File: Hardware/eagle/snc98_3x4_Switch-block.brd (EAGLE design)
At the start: 56.4 x 83.2 mm, 67 parts

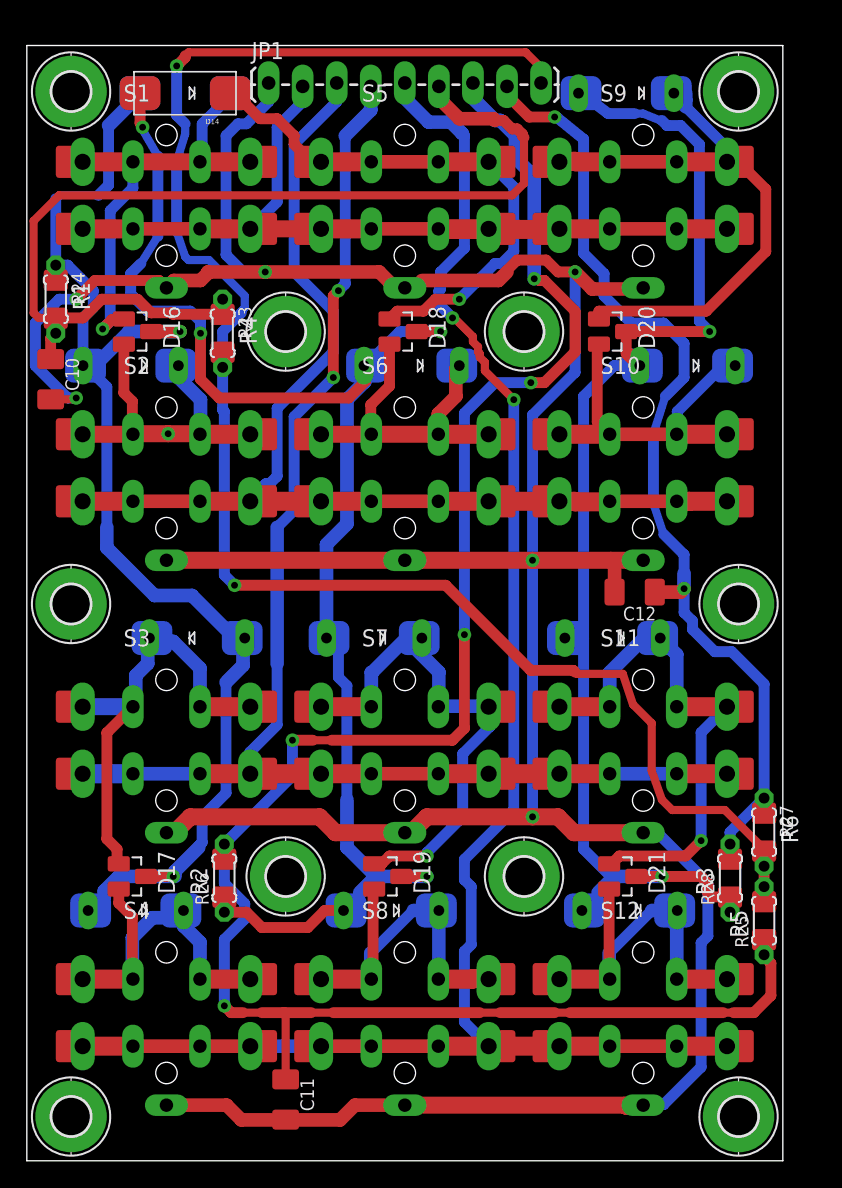
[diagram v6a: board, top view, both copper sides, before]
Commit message: new Switch Layout - with Kipptaster
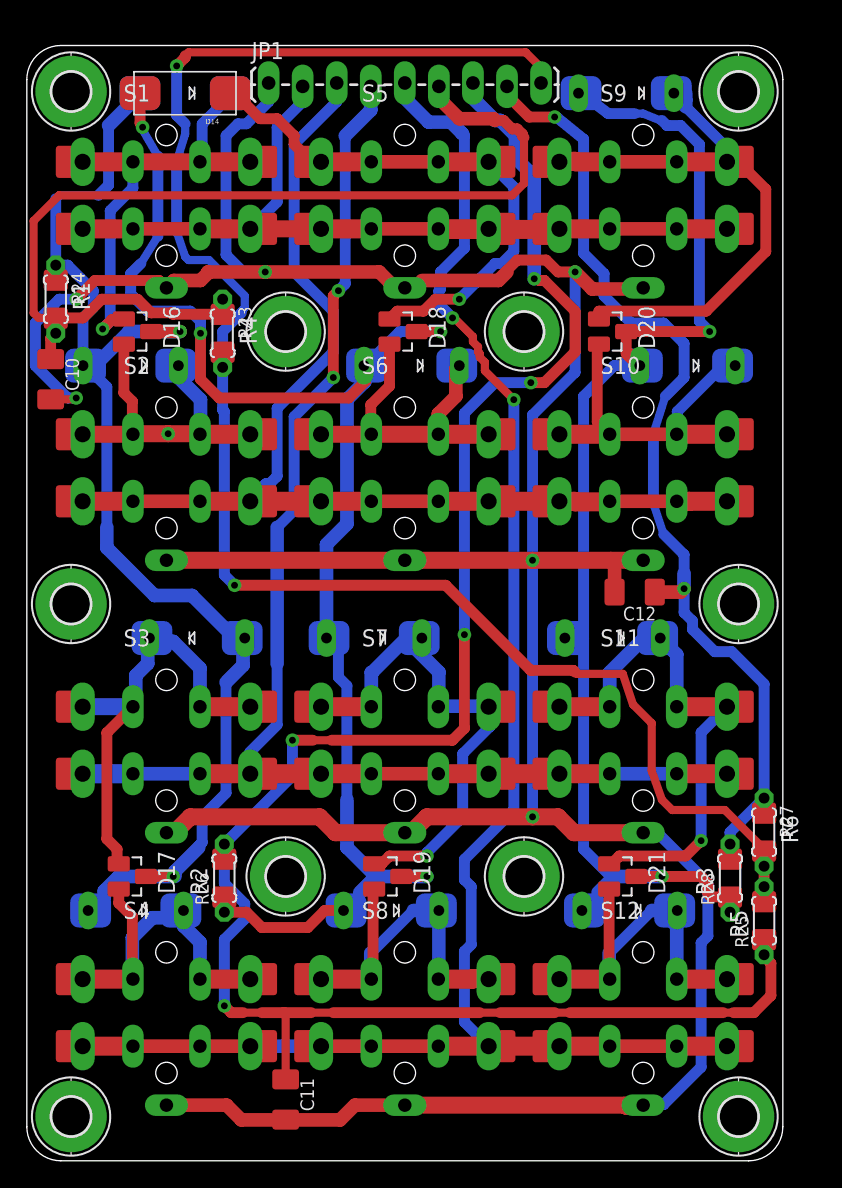
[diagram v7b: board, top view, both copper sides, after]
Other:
- outline, holes or cut-outs redrawn
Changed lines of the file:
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@@
 <setting verticaltext="up"/>
 </settings>
-<grid distance="5" unitdist="mil" unit="mil" style="dots" multiple="1" display="yes" altdistance="0.005" altunitdist="inch" altunit="inch"/>
+<grid distance="5" unitdist="mil" unit="mil" style="lines" multiple="1" display="yes" altdistance="0.01" altunitdist="inch" altunit="inch"/>
 <layers>
 <layer number="1" name="Top" color="4" fill="1" visible="yes" active="yes"/>
@@
 <board>
 <plain>
-<wire x1="0" y1="83.185" x2="0" y2="0" width="0" layer="20"/>
-<wire x1="0" y1="0" x2="56.388" y2="0" width="0" layer="20"/>
+<wire x1="0" y1="2.54" x2="0" y2="80.645" width="0" layer="20"/>
+<wire x1="2.54" y1="83.185" x2="53.848" y2="83.185" width="0" layer="20"/>
+<wire x1="56.388" y1="80.645" x2="56.388" y2="2.54" width="0" layer="20"/>
+<wire x1="2.54" y1="0" x2="53.848" y2="0" width="0" layer="20"/>
 <text x="7.874" y="42.164" size="1.27" layer="22" ratio="16" rot="MR180">snc98 3x4 Switch-block Rev. 0.3</text>
 <text x="37.846" y="42.545" size="1.27" layer="22" ratio="16" rot="MR0">CERN OHL    v.1.2 or later</text>
@@
 <text x="2.159" y="23.114" size="1.27" layer="22" ratio="16" rot="MR270" align="center">source</text>
 <text x="27.94" y="1.397" size="1.27" layer="22" ratio="16" rot="MR0" align="center">https://oshpark.com/profiles/Jens_G</text>
-<wire x1="0" y1="83.185" x2="56.388" y2="83.185" width="0" layer="20"/>
-<wire x1="56.388" y1="83.185" x2="56.388" y2="0" width="0" layer="20"/>
 <wire x1="27.3685" y1="19.1135" x2="27.3685" y2="18.2245" width="0.127" layer="21"/>
 <wire x1="27.3685" y1="18.2245" x2="27.7495" y2="18.669" width="0.127" layer="21"/>
@@
 <dimension x1="53.086" y1="3.302" x2="53.086" y2="41.529" x3="60.96" y3="22.4155" textsize="1.778" textratio="15" layer="47"/>
 <dimension x1="53.086" y1="3.302" x2="53.086" y2="79.756" x3="66.294" y3="41.529" textsize="1.778" textratio="15" layer="47"/>
+<wire x1="2.54" y1="83.185" x2="0" y2="80.645" width="0" layer="20" curve="90"/>
+<wire x1="56.388" y1="80.645" x2="53.848" y2="83.185" width="0" layer="20" curve="90"/>
+<wire x1="0" y1="2.54" x2="2.54" y2="0" width="0" layer="20" curve="90"/>
+<wire x1="53.848" y1="0" x2="56.388" y2="2.54" width="0" layer="20" curve="90"/>
 </plain>
 <attributes>
